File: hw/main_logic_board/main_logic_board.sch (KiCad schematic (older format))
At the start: 46 parts, among them J11 SPI1, J12 UART0, J13 UART2, J14 UART4, J15 I2C1, J16 I2C2, J4 USB_A, J5 RC_OUT_1, J6 RC_OUT_2, J7 RC_OUT_3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

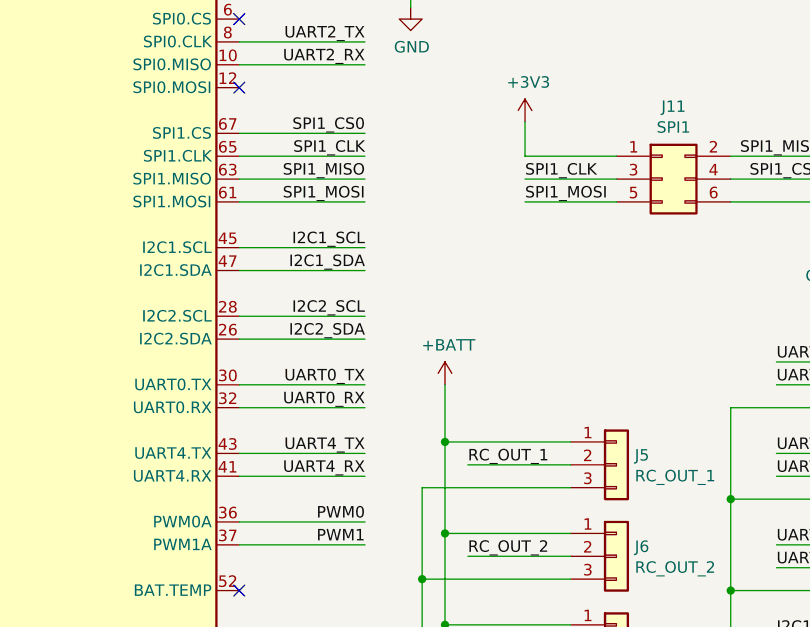
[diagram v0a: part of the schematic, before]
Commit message: Add more silk, + I2C pull ups
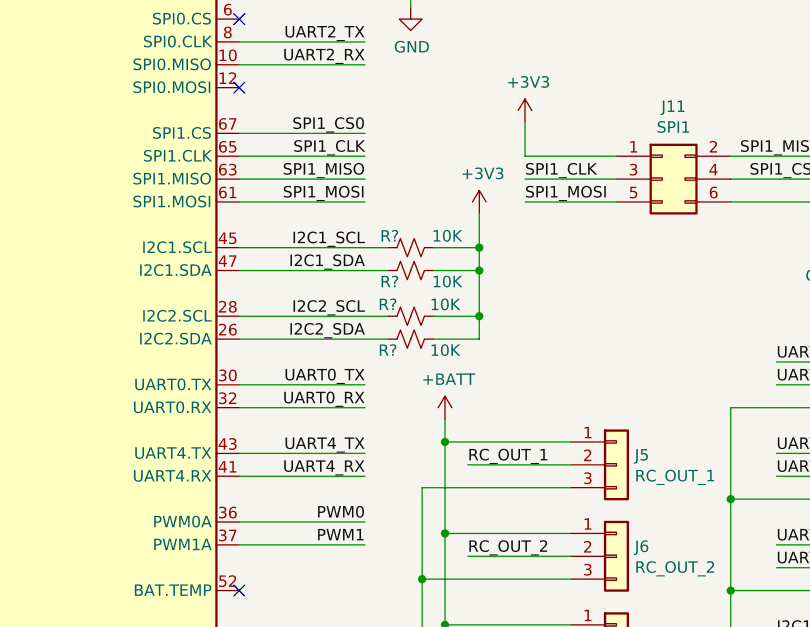
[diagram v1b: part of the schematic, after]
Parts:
- added R? (x4): 10K, Resistor_SMD:R_0805_2012Metric, symbol Device:R_Small_US
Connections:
- net +3V3: now also R?.1, R?.2, R?.2, R?.2
- net I2C1_SCL: now also R?.1
- net I2C1_SDA: now also R?.1
- net I2C2_SCL: now also R?.1
- net I2C2_SDA: now also R?.2
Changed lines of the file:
@@
 	1    0    0    -1
 $EndComp
-Wire Wire Line
-	7800 3700 8350 3700
-Wire Wire Line
-	7800 3800 8350 3800
 Text Label 8350 3700 2    50   ~ 0
 I2C2_SCL
@@
 Text Label 5300 3600 0    50   ~ 0
 AIN_1V8_1
-Wire Wire Line
-	7800 3400 8350 3400
-Wire Wire Line
-	7800 3500 8350 3500
 Text Label 8350 3400 2    50   ~ 0
 I2C1_SCL
@@
 RC_OUT_4
 Wire Wire Line
-	9250 4350 8800 4350
-Wire Wire Line
 	9250 4750 8800 4750
 Wire Wire Line
@@
 Wire Wire Line
 	8700 4650 8700 5050
-Wire Wire Line
-	8700 4250 8700 4000
-Connection ~ 8700 4250
 Wire Wire Line
 	8600 4450 8600 4850
@@
 L power:+BATT #PWR0138
 U 1 1 5EDA33F7
-P 8700 4000
-F 0 "#PWR0138" H 8700 3850 50  0001 C CNN
-F 1 "+BATT" H 8715 4173 50  0000 C CNN
-F 2 "" H 8700 4000 50  0001 C CNN
-F 3 "" H 8700 4000 50  0001 C CNN
-	1    8700 4000
+P 8700 4150
+F 0 "#PWR0138" H 8700 4000 50  0001 C CNN
+F 1 "+BATT" H 8715 4323 50  0000 C CNN
+F 2 "" H 8700 4150 50  0001 C CNN
+F 3 "" H 8700 4150 50  0001 C CNN
+	1    8700 4150
 	1    0    0    -1
 $EndComp
@@
 Connection ~ 7100 1100
 NoConn ~ 7100 1400
+$Comp
+L Device:R_Small_US R?
+U 1 1 5EC094BF
+P 8550 3700
+AR Path="/5E9DC864/5EC094BF" Ref="R?"  Part="1"
+AR Path="/5EC094BF" Ref="R?"  Part="1"
+F 0 "R?" V 8600 3800 50  0000 C CNN
+F 1 "10K" V 8600 3550 50  0000 C CNN
+F 2 "Resistor_SMD:R_0805_2012Metric" H 8550 3700 50  0001 C CNN
+F 3 "~" H 8550 3700 50  0001 C CNN
+	1    8550 3700
+	0    -1   -1   0
+$EndComp
+Wire Wire Line
+	8800 4350 9250 4350
+Wire Wire Line
+	8700 4250 8700 4150
+Connection ~ 8700 4250
+$Comp
+L Device:R_Small_US R?
+U 1 1 5EC5C35B
+P 8550 3800
+AR Path="/5E9DC864/5EC5C35B" Ref="R?"  Part="1"
+AR Path="/5EC5C35B" Ref="R?"  Part="1"
+F 0 "R?" V 8600 3700 50  0000 C CNN
+F 1 "10K" V 8600 3950 50  0000 C CNN
+F 2 "Resistor_SMD:R_0805_2012Metric" H 8550 3800 50  0001 C CNN
+F 3 "~" H 8550 3800 50  0001 C CNN
+	1    8550 3800
+	0    1    1    0
+$EndComp
+Wire Wire Line
+	7800 3700 8450 3700
+Wire Wire Line
+	7800 3800 8450 3800
+$Comp
+L Device:R_Small_US R?
+U 1 1 5ECCA759
+P 8550 3400
+AR Path="/5E9DC864/5ECCA759" Ref="R?"  Part="1"
+AR Path="/5ECCA759" Ref="R?"  Part="1"
+F 0 "R?" V 8600 3450 50  0000 L CNN
+F 1 "10K" V 8600 3175 50  0000 L CNN
+F 2 "Resistor_SMD:R_0805_2012Metric" H 8550 3400 50  0001 C CNN
+F 3 "~" H 8550 3400 50  0001 C CNN
+	1    8550 3400
+	0    -1   -1   0
+$EndComp
+$Comp
+L Device:R_Small_US R?
+U 1 1 5ECD61A0
+P 8550 3500
+AR Path="/5E9DC864/5ECD61A0" Ref="R?"  Part="1"
+AR Path="/5ECD61A0" Ref="R?"  Part="1"
+F 0 "R?" V 8500 3550 50  0000 L CNN
+F 1 "10K" V 8500 3275 50  0000 L CNN
+F 2 "Resistor_SMD:R_0805_2012Metric" H 8550 3500 50  0001 C CNN
+F 3 "~" H 8550 3500 50  0001 C CNN
+	1    8550 3500
+	0    -1   -1   0
+$EndComp
+Wire Wire Line
+	7800 3400 8450 3400
+Wire Wire Line
+	7800 3500 8450 3500
+Wire Wire Line
+	8650 3800 8850 3800
+Wire Wire Line
+	8850 3800 8850 3700
+Wire Wire Line
+	8650 3700 8850 3700
+Connection ~ 8850 3700
+Wire Wire Line
+	8850 3700 8850 3500
+Wire Wire Line
+	8650 3500 8850 3500
+Connection ~ 8850 3500
+Wire Wire Line
+	8850 3500 8850 3400
+Wire Wire Line
+	8650 3400 8850 3400
+Connection ~ 8850 3400
+Wire Wire Line
+	8850 3400 8850 3250
+$Comp
+L power:+3V3 #PWR?
+U 1 1 5ED2CB78
+P 8850 3250
+F 0 "#PWR?" H 8850 3100 50  0001 C CNN
+F 1 "+3V3" H 8865 3423 50  0000 C CNN
+F 2 "" H 8850 3250 50  0001 C CNN
+F 3 "" H 8850 3250 50  0001 C CNN
+	1    8850 3250
+	1    0    0    -1
+$EndComp
 $EndSCHEMATC
